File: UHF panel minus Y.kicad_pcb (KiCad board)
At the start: 4 copper layers, 331 x 82 mm, 30 parts, among them IC1 LMT84DCKT, J1 CONSMA001-SMD-G, J2 2pin_header, J3 2pin_header, J4 2pin_header, T1 NCS1.5-232+, U1 AQZ10X, U2 S16008-33

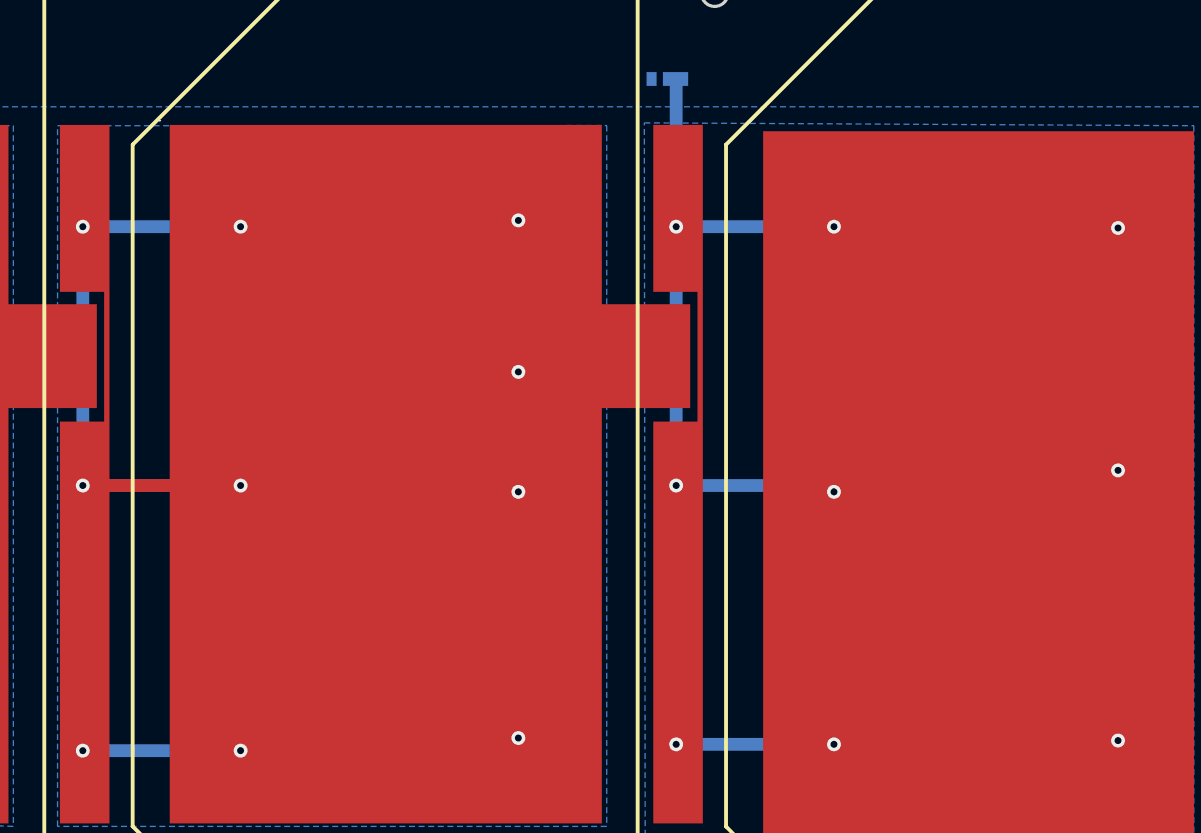
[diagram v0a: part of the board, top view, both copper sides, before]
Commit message: Fix solar cell connections
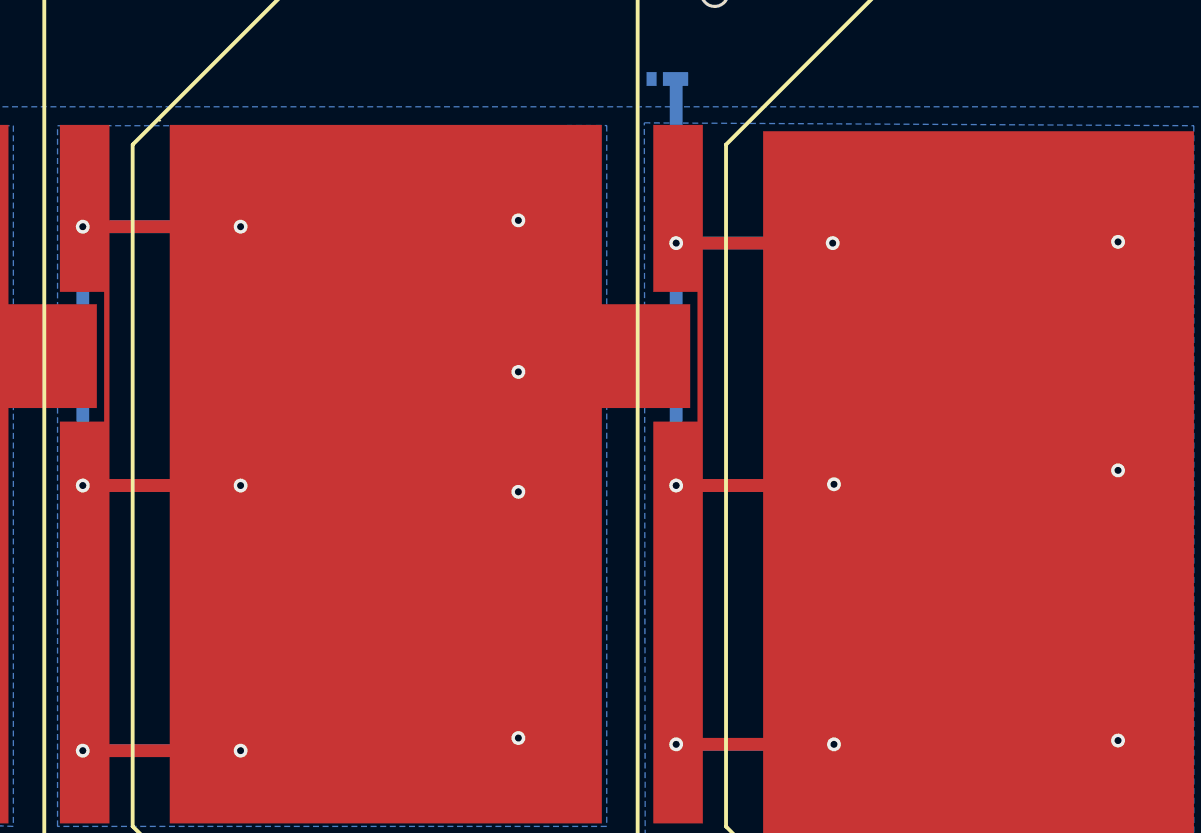
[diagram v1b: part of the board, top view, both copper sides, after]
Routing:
- net /VC: track 207.3 -> 243.0 mm
- net /VB: track 222.6 -> 247.6 mm
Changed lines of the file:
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@@
+	)
+	(segment
+		(start 136.58 161.36)
+		(end 149.08 161.36)
+		(width 1.016)
+		(layer "F.Cu")
+		(net 7)
 	)
 	(segment
@@
 	)
 	(segment
-		(start 149.08 141.36)
-		(end 149.58 140.86)
-		(width 1.016)
-		(layer "F.Cu")
-		(net 7)
-	)
-	(segment
 		(start 149.58 140.86)
 		(end 160.36 140.86)
@@
 		(net 7)
 	)
+	(segment
+		(start 136.58 121.66)
+		(end 148.98 121.66)
+		(width 1.016)
+		(layer "F.Cu")
+		(net 7)
+	)
+	(segment
+		(start 136.58 140.86)
+		(end 148.98 140.86)
+		(width 1.016)
+		(layer "F.Cu")
+		(net 7)
+	)
+	(segment
+		(start 149.48 140.76)
+		(end 149.58 140.86)
+		(width 1.016)
+		(layer "F.Cu")
+		(net 7)
+	)
+	(segment
+		(start 149.08 140.76)
+		(end 149.48 140.76)
+		(width 1.016)
+		(layer "F.Cu")
+		(net 7)
+	)
+	(segment
+		(start 148.98 140.86)
+		(end 149.08 140.76)
+		(width 1.016)
+		(layer "F.Cu")
+		(net 7)
+	)
 	(via
 		(at 171.58 139.66)
@@
 	)
 	(via
-		(at 171.58 120.46)
+		(at 171.58 121.56)
 		(size 1.1)
 		(drill 0.55)
@@
 	)
 	(via
-		(at 136.58 120.36)
-		(size 1.1)
-		(drill 0.55)
-		(layers "F.Cu" "B.Cu")
-		(net 7)
-	)
-	(via
-		(at 149.08 120.36)
-		(size 1.1)
-		(drill 0.55)
-		(layers "F.Cu" "B.Cu")
-		(net 7)
-	)
-	(via
-		(at 149.08 141.36)
+		(at 136.58 121.66)
+		(size 1.1)
+		(drill 0.55)
+		(layers "F.Cu" "B.Cu")
+		(net 7)
+	)
+	(via
+		(at 148.98 121.66)
+		(size 1.1)
+		(drill 0.55)
+		(layers "F.Cu" "B.Cu")
+		(net 7)
+	)
+	(via
+		(at 149.08 140.76)
 		(size 1.1)
 		(drill 0.55)
@@
 		(drill 0.55)
 		(layers "F.Cu" "B.Cu")
+		(net 7)
+	)
+	(segment
+		(start 148.58 140.86)
+		(end 136.58 140.86)
+		(width 1.016)
+		(layer "B.Cu")
+		(net 7)
+	)
+	(segment
+		(start 171.58 161.06)
+		(end 171.58 139.66)
+		(width 1.016)
+		(layer "B.Cu")
+		(net 7)
+	)
+	(segment
+		(start 136.58 140.86)
+		(end 136.58 121.66)
+		(width 1.016)
+		(layer "B.Cu")
+		(net 7)
+	)
+	(segment
+		(start 136.53 108.86)
+		(end 136.53 108.66)
+		(width 1.016)
+		(layer "B.Cu")
+		(net 7)
+	)
+	(segment
+		(start 149.08 140.76)
+		(end 149.08 121.76)
+		(width 1.016)
+		(layer "B.Cu")
+		(net 7)
+	)
+	(segment
+		(start 171.58 139.66)
+		(end 171.58 121.56)
+		(width 1.016)
+		(layer "B.Cu")
+		(net 7)
+	)
+	(segment
+		(start 136.58 161.36)
+		(end 136.58 140.86)
+		(width 1.016)
+		(layer "B.Cu")
 		(net 7)
 	)
@@
 	)
 	(segment
-		(start 149.08 141.36)
-		(end 149.08 120.36)
-		(width 1.016)
-		(layer "B.Cu")
-		(net 7)
-	)
-	(segment
-		(start 136.53 108.86)
-		(end 136.53 108.66)
-		(width 1.016)
-		(layer "B.Cu")
-		(net 7)
-	)
-	(segment
-		(start 171.58 120.46)
-		(end 170.18 119.06)
-		(width 1.016)
-		(layer "B.Cu")
-		(net 7)
-	)
-	(segment
-		(start 171.58 161.06)
-		(end 171.58 139.66)
+		(start 136.58 121.66)
+		(end 148.98 121.66)
+		(width 1.016)
+		(layer "B.Cu")
+		(net 7)
+	)
+	(segment
+		(start 171.58 121.56)
+		(end 169.08 119.06)
+		(width 1.016)
+		(layer "B.Cu")
+		(net 7)
+	)
+	(segment
+		(start 149.08 121.76)
+		(end 148.98 121.66)
+		(width 1.016)
+		(layer "B.Cu")
+		(net 7)
+	)
+	(segment
+		(start 169.08 119.06)
+		(end 151.58 119.06)
+		(width 1.016)
+		(layer "B.Cu")
+		(net 7)
+	)
+	(segment
+		(start 148.68 140.76)
+		(end 148.58 140.86)
 		(width 1.016)
 		(layer "B.Cu")
@@
 	(segment
 		(start 149.08 161.36)
-		(end 149.08 141.36)
+		(end 149.08 140.76)
+		(width 1.016)
+		(layer "B.Cu")
+		(net 7)
+	)
+	(segment
+		(start 136.58 121.66)
+		(end 136.58 108.91)
 		(width 1.016)
 		(layer "B.Cu")
@@
 	)
 	(segment
-		(start 136.58 140.86)
-		(end 136.58 120.36)
-		(width 1.016)
-		(layer "B.Cu")
-		(net 7)
-	)
-	(segment
-		(start 136.58 120.36)
-		(end 136.58 108.91)
-		(width 1.016)
-		(layer "B.Cu")
-		(net 7)
-	)
-	(segment
-		(start 136.58 161.36)
-		(end 136.58 140.86)
-		(width 1.016)
-		(layer "B.Cu")
-		(net 7)
-	)
-	(segment
-		(start 150.38 119.06)
-		(end 149.08 120.36)
-		(width 1.016)
-		(layer "B.Cu")
-		(net 7)
-	)
-	(segment
-		(start 136.58 120.36)
-		(end 149.08 120.36)
-		(width 1.016)
-		(layer "B.Cu")
-		(net 7)
-	)
-	(segment
-		(start 136.58 140.86)
-		(end 148.58 140.86)
-		(width 1.016)
-		(layer "B.Cu")
-		(net 7)
-	)
-	(segment
-		(start 170.18 119.06)
-		(end 150.38 119.06)
-		(width 1.016)
-		(layer "B.Cu")
-		(net 7)
-	)
-	(segment
-		(start 148.58 140.86)
-		(end 149.08 141.36)
-		(width 1.016)
-		(layer "B.Cu")
-		(net 7)
-	)
-	(segment
-		(start 171.58 139.66)
-		(end 171.58 120.46)
+		(start 149.08 140.76)
+		(end 148.68 140.76)
+		(width 1.016)
+		(layer "B.Cu")
+		(net 7)
+	)
+	(segment
+		(start 151.58 119.06)
+		(end 148.98 121.66)
 		(width 1.016)
 		(layer "B.Cu")
@@
 	)
 	(segment
+		(start 89.53 120.36)
+		(end 102.08 120.36)
+		(width 1.016)
+		(layer "F.Cu")
+		(net 13)
+	)
+	(segment
 		(start 112.17 140.86)
 		(end 113.31 139.72)
@@
 	)
 	(segment
+		(start 89.58 161.86)
+		(end 102.08 161.86)
+		(width 1.016)
+		(layer "F.Cu")
+		(net 13)
+	)
+	(segment
 		(start 102.08 140.86)
 		(end 112.17 140.86)
@@
 	)
 	(segment
+		(start 89.58 140.86)
+		(end 89.58 161.86)
+		(width 1.016)
+		(layer "B.Cu")
+		(net 13)
+	)
+	(segment
+		(start 102.08 161.86)
+		(end 102.08 140.86)
+		(width 1.016)
+		(layer "B.Cu")
+		(net 13)
+	)
+	(segment
+		(start 89.58 120.36)
+		(end 102.08 120.36)
+		(width 1.016)
+		(layer "B.Cu")
+		(net 13)
+	)
+	(segment
+		(start 124.08 160.86)
+		(end 124.08 141.36)
+		(width 1.016)
+		(layer "B.Cu")
+		(net 13)
+	)
+	(segment
 		(start 89.58 161.86)
 		(end 102.08 161.86)
 		(width 1.016)
 		(layer "B.Cu")
-		(net 13)
-	)
-	(segment
-		(start 89.58 140.86)
-		(end 89.58 161.86)
-		(width 1.016)
-		(layer "B.Cu")
-		(net 13)
-	)
-	(segment
-		(start 102.08 161.86)
-		(end 102.08 140.86)
-		(width 1.016)
-		(layer "B.Cu")
-		(net 13)
-	)
-	(segment
-		(start 89.58 120.36)
-		(end 102.08 120.36)
-		(width 1.016)
-		(layer "B.Cu")
-		(net 13)
-	)
-	(segment
-		(start 124.08 160.86)
-		(end 124.08 141.36)
-		(width 1.016)
-		(layer "B.Cu")
